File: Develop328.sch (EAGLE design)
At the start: 11 parts

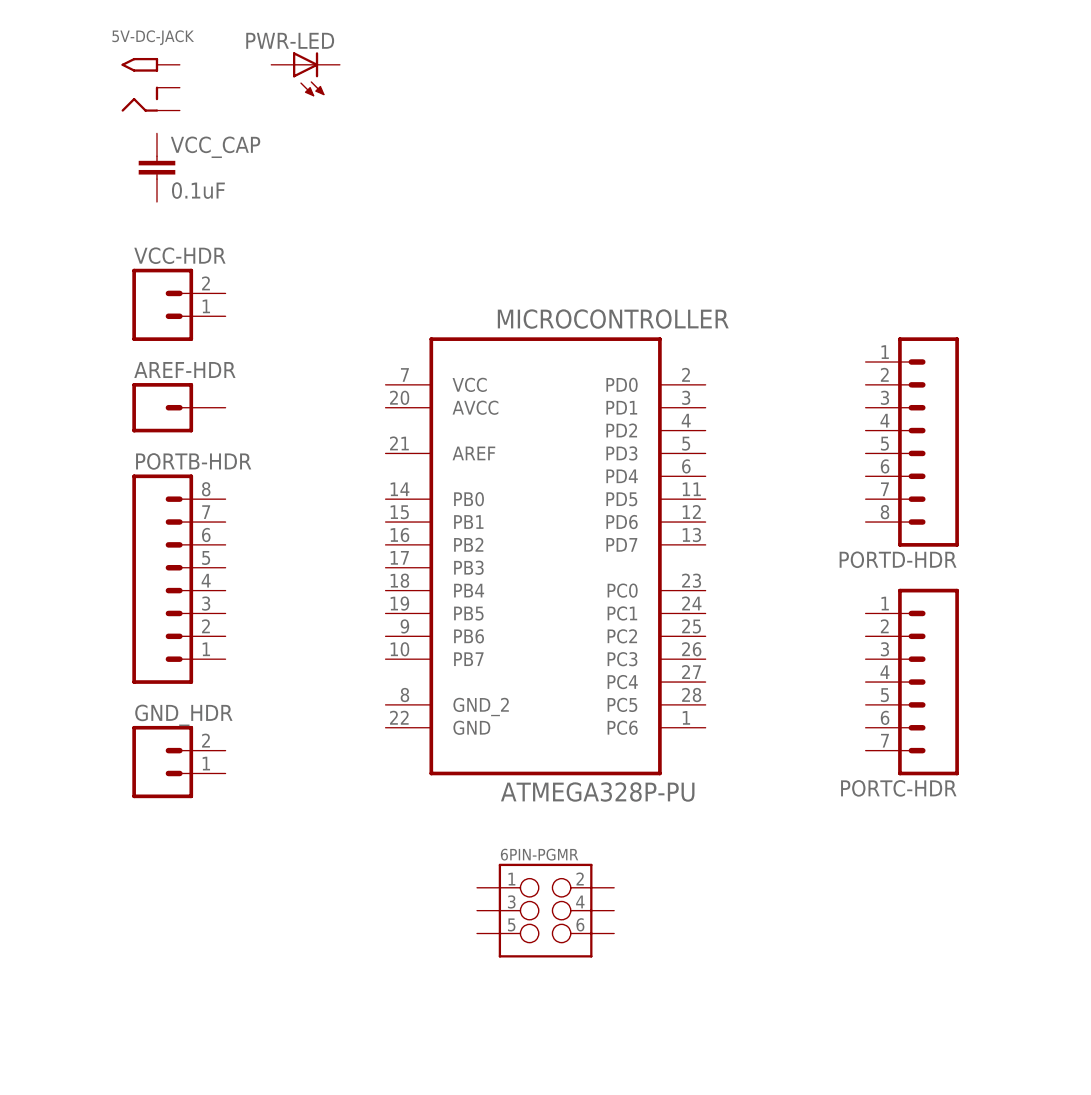
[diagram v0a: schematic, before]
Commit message: Added wires to all port headers
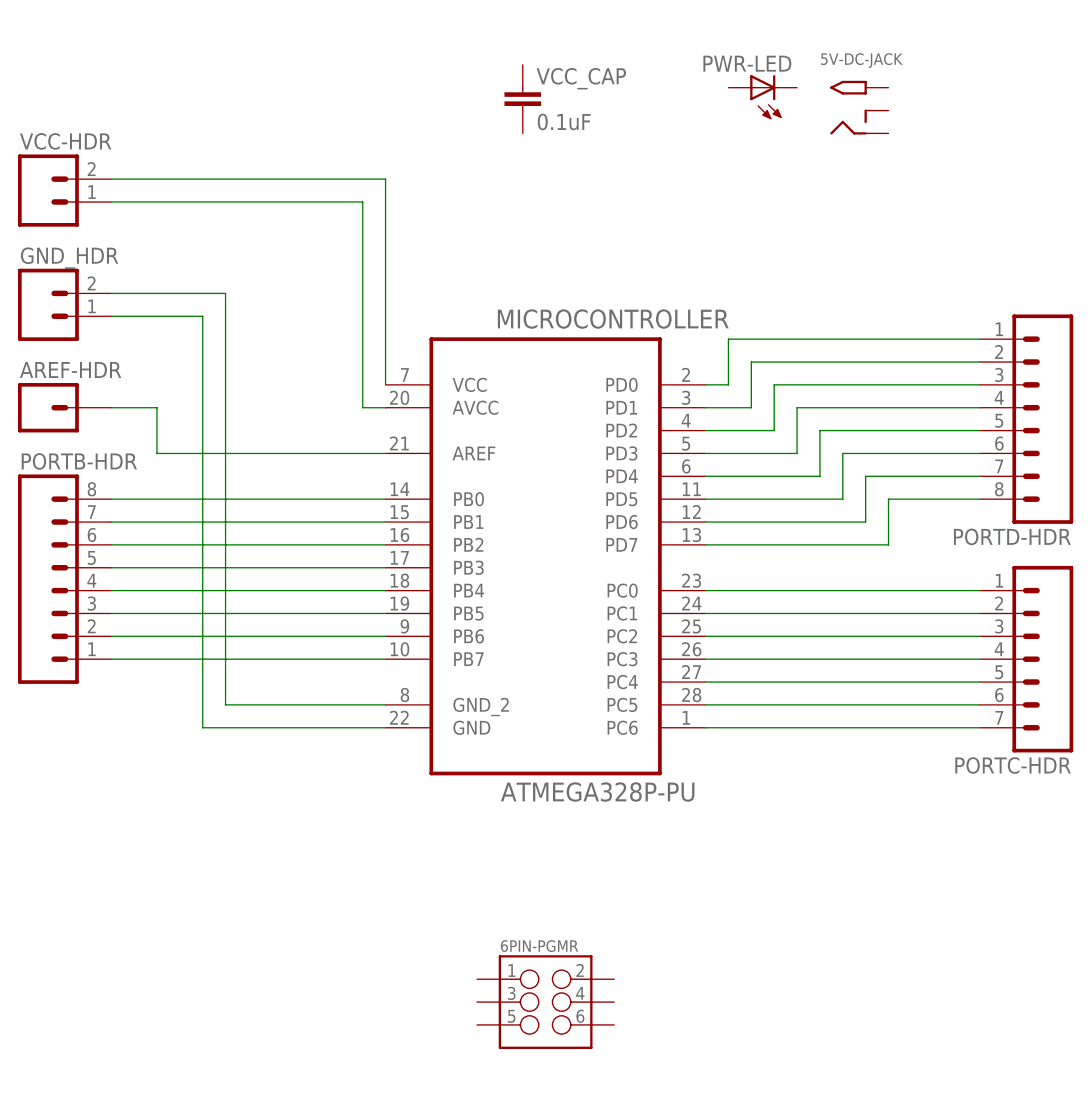
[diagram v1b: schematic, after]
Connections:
- new net N$1: MICROCONTROLLER.VCC, VCC-HDR.2
- new net N$10: MICROCONTROLLER.PD7, PORTD-HDR.8
- new net N$11: MICROCONTROLLER.PC0, PORTC-HDR.1
- new net N$12: MICROCONTROLLER.PC1, PORTC-HDR.2
- new net N$13: MICROCONTROLLER.PC2, PORTC-HDR.3
- new net N$14: MICROCONTROLLER.PC3, PORTC-HDR.4
- new net N$15: MICROCONTROLLER.PC4, PORTC-HDR.5
- new net N$16: MICROCONTROLLER.PC5, PORTC-HDR.6
- new net N$17: MICROCONTROLLER.PC6, PORTC-HDR.7
- new net N$18: MICROCONTROLLER.PB0, PORTB-HDR.8
- new net N$19: MICROCONTROLLER.PB1, PORTB-HDR.7
- new net N$2: GND_HDR.1, MICROCONTROLLER.GND
- new net N$20: MICROCONTROLLER.PB2, PORTB-HDR.6
- new net N$21: MICROCONTROLLER.PB3, PORTB-HDR.5
- new net N$22: MICROCONTROLLER.PB4, PORTB-HDR.4
- new net N$23: MICROCONTROLLER.PB5, PORTB-HDR.3
- new net N$24: MICROCONTROLLER.PB6, PORTB-HDR.2
- new net N$25: MICROCONTROLLER.PB7, PORTB-HDR.1
- new net N$26: AREF-HDR.1, MICROCONTROLLER.AREF
- new net N$27: MICROCONTROLLER.AVCC, VCC-HDR.1
- new net N$28: GND_HDR.2, MICROCONTROLLER.GND_2
- new net N$3: MICROCONTROLLER.PD0, PORTD-HDR.1
- new net N$4: MICROCONTROLLER.PD1, PORTD-HDR.2
- new net N$5: MICROCONTROLLER.PD2, PORTD-HDR.3
- new net N$6: MICROCONTROLLER.PD3, PORTD-HDR.4
- new net N$7: MICROCONTROLLER.PD4, PORTD-HDR.5
- new net N$8: MICROCONTROLLER.PD5, PORTD-HDR.6
- new net N$9: MICROCONTROLLER.PD6, PORTD-HDR.7
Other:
- moved on the sheet: 5V-DC-JACK, 6PIN-PGMR, AREF-HDR, GND_HDR, PORTB-HDR, PORTC-HDR, PORTD-HDR, PWR-LED, VCC-HDR, VCC_CAP

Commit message: Replaced wires with electrical connections
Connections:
- removed net N$1 (its old number): MICROCONTROLLER.VCC, VCC-HDR.2
- removed net N$2 (its old number): GND_HDR.1, MICROCONTROLLER.GND
- removed net N$27: MICROCONTROLLER.AVCC, VCC-HDR.1
- removed net N$28: GND_HDR.2, MICROCONTROLLER.GND_2
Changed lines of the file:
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@@
 </busses>
 <nets>
-<net name="N$2" class="0">
-<segment>
-<pinref part="MICROCONTROLLER" gate="A" pin="GND"/>
-<wire x1="48.26" y1="25.4" x2="27.94" y2="25.4" width="0.1524" layer="91"/>
-<pinref part="GND_HDR" gate="G$1" pin="1"/>
-<wire x1="27.94" y1="25.4" x2="27.94" y2="71.12" width="0.1524" layer="91"/>
-<wire x1="27.94" y1="71.12" x2="17.78" y2="71.12" width="0.1524" layer="91"/>
-</segment>
-</net>
-<net name="N$18" class="0">
+<net name="N$1" class="0">
 <segment>
 <pinref part="PORTB-HDR" gate="G$1" pin="8"/>
@@
 </segment>
 </net>
-<net name="N$19" class="0">
+<net name="N$2" class="0">
 <segment>
 <pinref part="PORTB-HDR" gate="G$1" pin="7"/>
@@
 </segment>
 </net>
-<net name="N$20" class="0">
+<net name="N$3" class="0">
 <segment>
 <pinref part="PORTB-HDR" gate="G$1" pin="6"/>
@@
 </segment>
 </net>
-<net name="N$21" class="0">
+<net name="N$4" class="0">
 <segment>
 <pinref part="PORTB-HDR" gate="G$1" pin="5"/>
@@
 </segment>
 </net>
-<net name="N$22" class="0">
+<net name="N$5" class="0">
 <segment>
 <pinref part="PORTB-HDR" gate="G$1" pin="4"/>
@@
 </segment>
 </net>
-<net name="N$23" class="0">
+<net name="N$6" class="0">
 <segment>
 <pinref part="PORTB-HDR" gate="G$1" pin="3"/>
@@
 </segment>
 </net>
-<net name="N$24" class="0">
+<net name="N$7" class="0">
 <segment>
 <pinref part="PORTB-HDR" gate="G$1" pin="2"/>
@@
 </segment>
 </net>
-<net name="N$25" class="0">
+<net name="N$8" class="0">
 <segment>
 <pinref part="PORTB-HDR" gate="G$1" pin="1"/>
@@
 </segment>
 </net>
-<net name="N$11" class="0">
+<net name="N$9" class="0">
 <segment>
 <pinref part="PORTC-HDR" gate="G$1" pin="1"/>
@@
 </segment>
 </net>
-<net name="N$12" class="0">
+<net name="N$10" class="0">
 <segment>
 <pinref part="PORTC-HDR" gate="G$1" pin="2"/>
@@
 </segment>
 </net>
-<net name="N$13" class="0">
+<net name="N$11" class="0">
 <segment>
 <pinref part="PORTC-HDR" gate="G$1" pin="3"/>
@@
 </segment>
 </net>
-<net name="N$15" class="0">
+<net name="N$12" class="0">
+<segment>
+<pinref part="PORTC-HDR" gate="G$1" pin="4"/>
+<pinref part="MICROCONTROLLER" gate="A" pin="PC3"/>
+<wire x1="114.3" y1="33.02" x2="83.82" y2="33.02" width="0.1524" layer="91"/>
+</segment>
+</net>
+<net name="N$13" class="0">
 <segment>
 <pinref part="PORTC-HDR" gate="G$1" pin="5"/>
@@
 </segment>
 </net>
-<net name="N$16" class="0">
+<net name="N$14" class="0">
 <segment>
 <pinref part="PORTC-HDR" gate="G$1" pin="6"/>
@@
 </segment>
 </net>
-<net name="N$17" class="0">
+<net name="N$15" class="0">
 <segment>
 <pinref part="PORTC-HDR" gate="G$1" pin="7"/>
@@
 </segment>
 </net>
-<net name="N$3" class="0">
+<net name="N$16" class="0">
 <segment>
 <pinref part="PORTD-HDR" gate="G$1" pin="1"/>
@@
 </segment>
 </net>
-<net name="N$4" class="0">
+<net name="N$17" class="0">
 <segment>
 <pinref part="PORTD-HDR" gate="G$1" pin="2"/>
@@
 </segment>
 </net>
-<net name="N$5" class="0">
+<net name="N$18" class="0">
 <segment>
 <pinref part="PORTD-HDR" gate="G$1" pin="3"/>
@@
 </segment>
 </net>
-<net name="N$6" class="0">
+<net name="N$19" class="0">
 <segment>
 <pinref part="PORTD-HDR" gate="G$1" pin="4"/>
@@
 </segment>
 </net>
-<net name="N$7" class="0">
+<net name="N$20" class="0">
 <segment>
 <pinref part="PORTD-HDR" gate="G$1" pin="5"/>
@@
 </segment>
 </net>
-<net name="N$8" class="0">
+<net name="N$21" class="0">
 <segment>
 <pinref part="PORTD-HDR" gate="G$1" pin="6"/>
@@
 </segment>
 </net>
-<net name="N$9" class="0">
+<net name="N$22" class="0">
 <segment>
 <pinref part="PORTD-HDR" gate="G$1" pin="7"/>
@@
 </segment>
 </net>
-<net name="N$10" class="0">
+<net name="N$23" class="0">
 <segment>
 <pinref part="PORTD-HDR" gate="G$1" pin="8"/>
@@
 </segment>
 </net>
-<net name="N$26" class="0">
+<net name="N$24" class="0">
 <segment>
 <pinref part="AREF-HDR" gate="G$1" pin="1"/>
 <wire x1="17.78" y1="60.96" x2="22.86" y2="60.96" width="0.1524" layer="91"/>
+<wire x1="22.86" y1="60.96" x2="22.86" y2="55.88" width="0.1524" layer="91"/>
 <pinref part="MICROCONTROLLER" gate="A" pin="AREF"/>
-<wire x1="22.86" y1="60.96" x2="22.86" y2="55.88" width="0.1524" layer="91"/>
 <wire x1="22.86" y1="55.88" x2="48.26" y2="55.88" width="0.1524" layer="91"/>
 </segment>
 </net>
-<net name="N$1" class="0">
-<segment>
-<pinref part="MICROCONTROLLER" gate="A" pin="VCC"/>
-<wire x1="48.26" y1="63.5" x2="48.26" y2="86.36" width="0.1524" layer="91"/>
-<pinref part="VCC-HDR" gate="G$1" pin="2"/>
-<wire x1="48.26" y1="86.36" x2="17.78" y2="86.36" width="0.1524" layer="91"/>
-</segment>
-</net>
-<net name="N$27" class="0">
-<segment>
-<pinref part="MICROCONTROLLER" gate="A" pin="AVCC"/>
-<wire x1="48.26" y1="60.96" x2="45.72" y2="60.96" width="0.1524" layer="91"/>
-<wire x1="45.72" y1="60.96" x2="45.72" y2="83.82" width="0.1524" layer="91"/>
-<pinref part="VCC-HDR" gate="G$1" pin="1"/>
-<wire x1="45.72" y1="83.82" x2="17.78" y2="83.82" width="0.1524" layer="91"/>
-</segment>
-</net>
-<net name="N$28" class="0">
-<segment>
-<pinref part="MICROCONTROLLER" gate="A" pin="GND_2"/>
-<wire x1="48.26" y1="27.94" x2="30.48" y2="27.94" width="0.1524" layer="91"/>
-<pinref part="GND_HDR" gate="G$1" pin="2"/>
-<wire x1="30.48" y1="27.94" x2="30.48" y2="73.66" width="0.1524" layer="91"/>
-<wire x1="30.48" y1="73.66" x2="17.78" y2="73.66" width="0.1524" layer="91"/>
-</segment>
-</net>
-<net name="N$14" class="0">
-<segment>
-<pinref part="PORTC-HDR" gate="G$1" pin="4"/>
-<pinref part="MICROCONTROLLER" gate="A" pin="PC3"/>
-<wire x1="114.3" y1="33.02" x2="83.82" y2="33.02" width="0.1524" layer="91"/>
-</segment>
-</net>

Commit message: Added GND and VCC nets and wired up the 6 pin programmer
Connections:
- new net GND: 6PIN-PGMR.2, GND_HDR.1, GND_HDR.2, MICROCONTROLLER.GND, MICROCONTROLLER.GND_2
- new net N$25: MICROCONTROLLER.AVCC, VCC-HDR.1
- new net VCC: 6PIN-PGMR.6, MICROCONTROLLER.VCC, VCC-HDR.2
- net N$10: now also 6PIN-PGMR.3
- net N$11: now also 6PIN-PGMR.5
- net N$12: now also 6PIN-PGMR.4
- net N$15: now also 6PIN-PGMR.1
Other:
- moved on the sheet: 6PIN-PGMR
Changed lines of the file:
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@@
 <part name="AREF-HDR" library="SparkFun-Connectors" deviceset="M01" device="PTH"/>
 <part name="VCC_CAP" library="SparkFun-Capacitors" deviceset="0.1UF-16V(+-10%)(0402)" device="" value="0.1uF"/>
+<part name="GND1" library="supply1" deviceset="GND" device=""/>
+<part name="GND2" library="supply1" deviceset="GND" device=""/>
+<part name="GND3" library="supply1" deviceset="GND" device=""/>
+<part name="GND4" library="supply1" deviceset="GND" device=""/>
+<part name="GND5" library="supply1" deviceset="GND" device=""/>
+<part name="P+1" library="supply1" deviceset="VCC" device=""/>
+<part name="P+3" library="supply1" deviceset="VCC" device=""/>
+<part name="P+4" library="supply1" deviceset="VCC" device=""/>
+<part name="P+2" library="supply1" deviceset="VCC" device=""/>
 </parts>
 <sheets>
@@
 <instance part="5V-DC-JACK" gate="G$1" x="99.06" y="93.98"/>
 <instance part="PWR-LED" gate="G$1" x="88.9" y="96.52" rot="R90"/>
-<instance part="6PIN-PGMR" gate="G$1" x="66.04" y="-5.08"/>
+<instance part="6PIN-PGMR" gate="G$1" x="91.44" y="-5.08"/>
 <instance part="PORTD-HDR" gate="G$1" x="119.38" y="60.96" rot="R180"/>
 <instance part="PORTB-HDR" gate="G$1" x="12.7" y="40.64"/>
@@
 <instance part="AREF-HDR" gate="G$1" x="10.16" y="60.96"/>
 <instance part="VCC_CAP" gate="G$1" x="63.5" y="93.98"/>
+<instance part="GND1" gate="1" x="40.64" y="27.94" rot="R270"/>
+<instance part="GND2" gate="1" x="43.18" y="22.86"/>
+<instance part="GND3" gate="1" x="101.6" y="0" rot="R180"/>
+<instance part="GND4" gate="1" x="25.4" y="76.2" rot="R180"/>
+<instance part="GND5" gate="1" x="25.4" y="68.58"/>
+<instance part="P+1" gate="VCC" x="22.86" y="86.36" rot="R270"/>
+<instance part="P+3" gate="VCC" x="93.98" y="86.36"/>
+<instance part="P+4" gate="VCC" x="101.6" y="-10.16" rot="R180"/>
+<instance part="P+2" gate="VCC" x="45.72" y="68.58"/>
 </instances>
 <busses>
@@
 <pinref part="PORTC-HDR" gate="G$1" pin="2"/>
 <pinref part="MICROCONTROLLER" gate="A" pin="PC1"/>
-<wire x1="114.3" y1="38.1" x2="83.82" y2="38.1" width="0.1524" layer="91"/>
+<wire x1="114.3" y1="38.1" x2="101.6" y2="38.1" width="0.1524" layer="91"/>
+<pinref part="6PIN-PGMR" gate="G$1" pin="3"/>
+<wire x1="101.6" y1="38.1" x2="83.82" y2="38.1" width="0.1524" layer="91"/>
+<wire x1="83.82" y1="-5.08" x2="81.28" y2="-5.08" width="0.1524" layer="91"/>
+<wire x1="81.28" y1="-5.08" x2="81.28" y2="7.62" width="0.1524" layer="91"/>
+<wire x1="81.28" y1="7.62" x2="101.6" y2="7.62" width="0.1524" layer="91"/>
+<wire x1="101.6" y1="7.62" x2="101.6" y2="38.1" width="0.1524" layer="91"/>
+<junction x="101.6" y="38.1"/>
 </segment>
 </net>
@@
 <pinref part="PORTC-HDR" gate="G$1" pin="3"/>
 <pinref part="MICROCONTROLLER" gate="A" pin="PC2"/>
-<wire x1="114.3" y1="35.56" x2="83.82" y2="35.56" width="0.1524" layer="91"/>
+<wire x1="114.3" y1="35.56" x2="99.06" y2="35.56" width="0.1524" layer="91"/>
+<pinref part="6PIN-PGMR" gate="G$1" pin="5"/>
+<wire x1="99.06" y1="35.56" x2="83.82" y2="35.56" width="0.1524" layer="91"/>
+<wire x1="83.82" y1="-7.62" x2="78.74" y2="-7.62" width="0.1524" layer="91"/>
+<wire x1="78.74" y1="-7.62" x2="78.74" y2="10.16" width="0.1524" layer="91"/>
+<wire x1="78.74" y1="10.16" x2="99.06" y2="10.16" width="0.1524" layer="91"/>
+<wire x1="99.06" y1="10.16" x2="99.06" y2="35.56" width="0.1524" layer="91"/>
+<junction x="99.06" y="35.56"/>
 </segment>
 </net>
@@
 <pinref part="PORTC-HDR" gate="G$1" pin="4"/>
 <pinref part="MICROCONTROLLER" gate="A" pin="PC3"/>
-<wire x1="114.3" y1="33.02" x2="83.82" y2="33.02" width="0.1524" layer="91"/>
+<wire x1="114.3" y1="33.02" x2="106.68" y2="33.02" width="0.1524" layer="91"/>
+<pinref part="6PIN-PGMR" gate="G$1" pin="4"/>
+<wire x1="106.68" y1="33.02" x2="83.82" y2="33.02" width="0.1524" layer="91"/>
+<wire x1="99.06" y1="-5.08" x2="106.68" y2="-5.08" width="0.1524" layer="91"/>
+<wire x1="106.68" y1="-5.08" x2="106.68" y2="33.02" width="0.1524" layer="91"/>
+<junction x="106.68" y="33.02"/>
 </segment>
 </net>
@@
 <pinref part="PORTC-HDR" gate="G$1" pin="7"/>
 <pinref part="MICROCONTROLLER" gate="A" pin="PC6"/>
-<wire x1="114.3" y1="25.4" x2="83.82" y2="25.4" width="0.1524" layer="91"/>
+<wire x1="114.3" y1="25.4" x2="104.14" y2="25.4" width="0.1524" layer="91"/>
+<pinref part="6PIN-PGMR" gate="G$1" pin="1"/>
+<wire x1="104.14" y1="25.4" x2="83.82" y2="25.4" width="0.1524" layer="91"/>
+<wire x1="83.82" y1="-2.54" x2="83.82" y2="5.08" width="0.1524" layer="91"/>
+<wire x1="83.82" y1="5.08" x2="104.14" y2="5.08" width="0.1524" layer="91"/>
+<wire x1="104.14" y1="5.08" x2="104.14" y2="25.4" width="0.1524" layer="91"/>
+<junction x="104.14" y="25.4"/>
 </segment>
 </net>
@@
 </segment>
 </net>
+<net name="GND" class="0">
+<segment>
+<pinref part="6PIN-PGMR" gate="G$1" pin="2"/>
+<pinref part="GND3" gate="1" pin="GND"/>
+<wire x1="99.06" y1="-2.54" x2="101.6" y2="-2.54" width="0.1524" layer="91"/>
+</segment>
+<segment>
+<pinref part="GND_HDR" gate="G$1" pin="2"/>
+<pinref part="GND4" gate="1" pin="GND"/>
+<wire x1="17.78" y1="73.66" x2="25.4" y2="73.66" width="0.1524" layer="91"/>
+</segment>
+<segment>
+<pinref part="GND_HDR" gate="G$1" pin="1"/>
+<pinref part="GND5" gate="1" pin="GND"/>
+<wire x1="17.78" y1="71.12" x2="25.4" y2="71.12" width="0.1524" layer="91"/>
+</segment>
+<segment>
+<pinref part="MICROCONTROLLER" gate="A" pin="GND_2"/>
+<pinref part="GND1" gate="1" pin="GND"/>
+<wire x1="48.26" y1="27.94" x2="43.18" y2="27.94" width="0.1524" layer="91"/>
+</segment>
+<segment>
+<pinref part="MICROCONTROLLER" gate="A" pin="GND"/>
+<pinref part="GND2" gate="1" pin="GND"/>
+<wire x1="48.26" y1="25.4" x2="43.18" y2="25.4" width="0.1524" layer="91"/>
+</segment>
+</net>
+<net name="VCC" class="0">
+<segment>
+<pinref part="6PIN-PGMR" gate="G$1" pin="6"/>
+<pinref part="P+4" gate="VCC" pin="VCC"/>
+<wire x1="99.06" y1="-7.62" x2="101.6" y2="-7.62" width="0.1524" layer="91"/>
+</segment>
+<segment>
+<pinref part="VCC-HDR" gate="G$1" pin="2"/>
+<pinref part="P+1" gate="VCC" pin="VCC"/>
+<wire x1="17.78" y1="86.36" x2="20.32" y2="86.36" width="0.1524" layer="91"/>
+</segment>
+<segment>
+<pinref part="P+2" gate="VCC" pin="VCC"/>
+<wire x1="45.72" y1="66.04" x2="45.72" y2="63.5" width="0.1524" layer="91"/>
+<pinref part="MICROCONTROLLER" gate="A" pin="VCC"/>
+<wire x1="45.72" y1="63.5" x2="48.26" y2="63.5" width="0.1524" layer="91"/>
+</segment>
+</net>
+<net name="N$25" class="0">
+<segment>
+<pinref part="VCC-HDR" gate="G$1" pin="1"/>
+<wire x1="17.78" y1="83.82" x2="35.56" y2="83.82" width="0.1524" layer="91"/>
+<wire x1="35.56" y1="83.82" x2="35.56" y2="60.96" width="0.1524" layer="91"/>
+<pinref part="MICROCONTROLLER" gate="A" pin="AVCC"/>
+<wire x1="35.56" y1="60.96" x2="48.26" y2="60.96" width="0.1524" layer="91"/>
+</segment>
+</net>
